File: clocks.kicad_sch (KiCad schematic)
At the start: 19 parts, among them J3 U_FL-R-SMT_10_, U42 CDCE906PWR, Y5 ABM8G-12.000MHZ-18-D2Y-T, Y6 AX3DCF1-200.0000

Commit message: Updated local libraries
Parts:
- J3: footprint antmicro-footprints:Coax_Conn_U.FL -> K410T-devboard-footprints:Coax_Conn_U.FL; symbol antmicroCoaxialConnectorsRF:U_FL-R-SMT_10_ -> K410T-devboard:U_FL-R-SMT_10_

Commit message: Bump revision to 1.0.0. Update name on schematic and PCB sheets
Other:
- title: K410T devboard -> Kintex 410T devboard

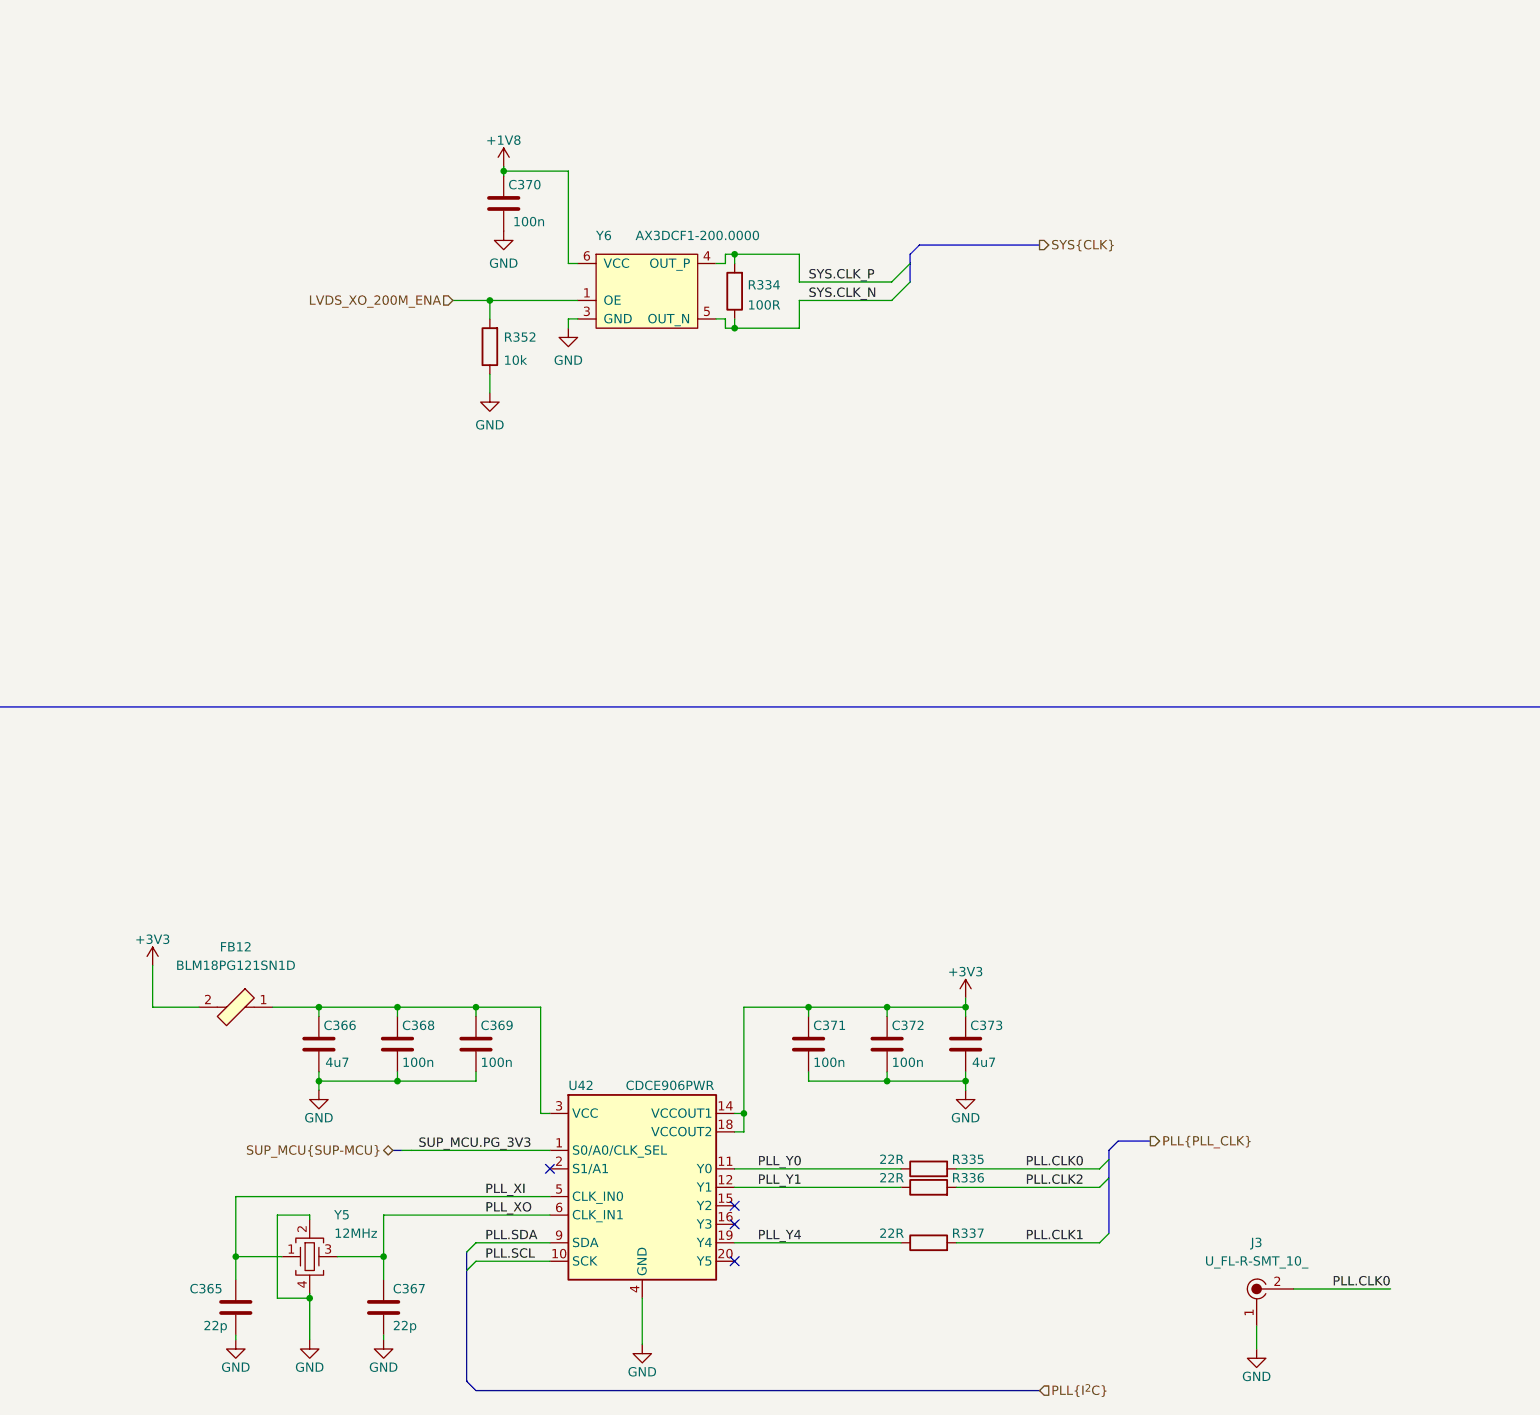
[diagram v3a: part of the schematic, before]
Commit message: Introduce component standardization
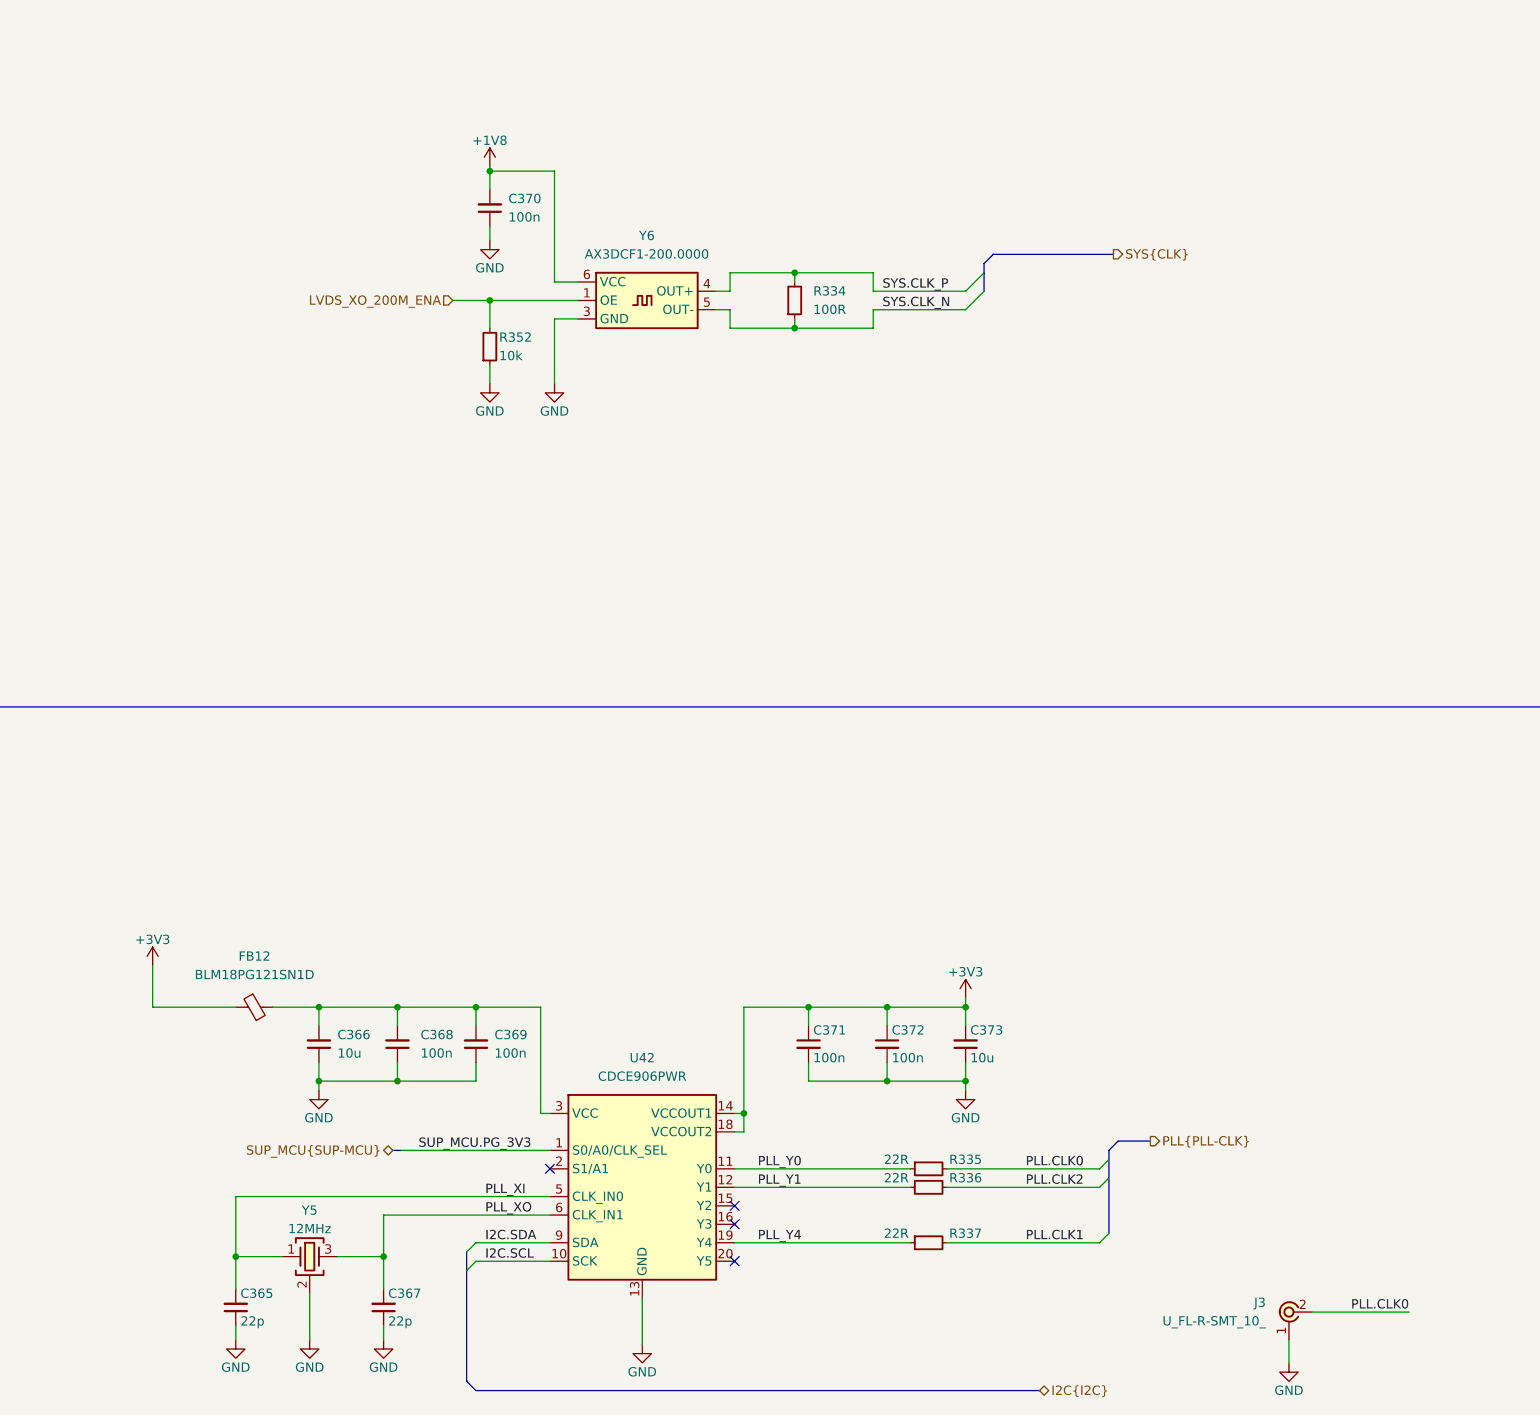
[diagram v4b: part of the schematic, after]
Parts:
- removed C366, C373: C_4u7_0201, K410T-devboard-footprints:0201-cap, symbol K410T-devboard:C_4u7_0201
- added C366, C373: C_10u_0402, K410T-devboard-footprints:C_0402_1005Metric, symbol K410T-devboard:C_10u_0402
- C365, C367: footprint K410T-devboard-footprints:0402-cap -> K410T-devboard-footprints:C_0402_1005Metric; Author (none) -> Antmicro; License (none) -> Apache-2.0; Manufacturer YAGEO -> Yaego
- C368, C369, C370, C371, C372: footprint K410T-devboard-footprints:0402-cap -> K410T-devboard-footprints:C_0402_1005Metric; Author (none) -> Antmicro; Dielectric (none) -> X5R; License (none) -> Apache-2.0; Voltage (none) -> 50V
- FB12: value BLM18PG121SN1D -> FB_120Z_2A_0603; footprint K410T-devboard-footprints:0603-res -> K410T-devboard-footprints:FB_0603_1608Metric; symbol K410T-devboard:BLM18PG121SN1D -> K410T-devboard:FB_120Z_2A_0603; Author (none) -> Antmicro; License (none) -> Apache-2.0; Manufacturer Murata Electronics North America -> Murata
- J3: Author (none) -> Antmicro; License (none) -> Apache-2.0; Manufacturer Hirose Electric Co Ltd -> Hirose
- R334: footprint K410T-devboard-footprints:0402-res -> K410T-devboard-footprints:R_0402_1005Metric; Author (none) -> Antmicro; License (none) -> Apache-2.0; Manufacturer BOURNS -> Bourns; Tolerance (none) -> 1%
- R335, R336, R337: footprint K410T-devboard-footprints:0402-res -> K410T-devboard-footprints:R_0402_1005Metric; Author (none) -> Antmicro; License (none) -> Apache-2.0; MPN CRCW040222R0FKED -> CR0402-FX-22R0GLF; Manufacturer VISHAY -> Bourns; Tolerance (none) -> 1%
- R352: footprint K410T-devboard-footprints:0402-res -> K410T-devboard-footprints:R_0402_1005Metric; Author (none) -> Antmicro; License (none) -> Apache-2.0; MPN CRCW040210K0FKEDHP -> CR0402-FX-1002GLF; Manufacturer VISHAY -> Bourns; Tolerance (none) -> 1%
- U42: Author (none) -> Antmicro; License (none) -> Apache-2.0
- Y5: value ABM8G-12.000MHZ-18-D2Y-T -> Oscillator_SMD_12MHz_KX-7; footprint K410T-devboard-footprints:KX-7 -> K410T-devboard-footprints:Oscillator_SMD_Geyer_KX-7-4Pin_3.2x2.5mm; symbol K410T-devboard:ABM8G-12.000MHZ-18-D2Y-T -> K410T-devboard:Oscillator_SMD_12MHz_KX-7; Author (none) -> Antmicro; License (none) -> Apache-2.0
- Y6: footprint K410T-devboard-footprints:AX3DAF1 -> K410T-devboard-footprints:Oscillator_SMD_Abracon_AX3_3.2x2.5x1mm; Author (none) -> Antmicro; License (none) -> Apache-2.0; Manufacturer ABRACON -> Abracon
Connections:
- net +1V8: now also C370.2; no longer C370.1
- net +3V3: now also C373.2
- net GND: now also C365.1, C367.1, C368.1, C369.1, C370.1, C366.1, C373.1; no longer C365.2, C367.2, C368.2, C369.2, C370.2
- net PLL_XI: now also C365.2; no longer C365.1
- net PLL_XO: now also C367.2; no longer C367.1
- net at FB12.1, U42.3 (VCC), U42.7 (VCC): now also C368.2, C369.2, C366.2; no longer C368.1, C369.1
- net PLL.SCL renamed I2C.SCL
- net PLL.SDA renamed I2C.SDA
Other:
- moved on the sheet: C365, C367, C368, C369, C370, C371, C372, R334

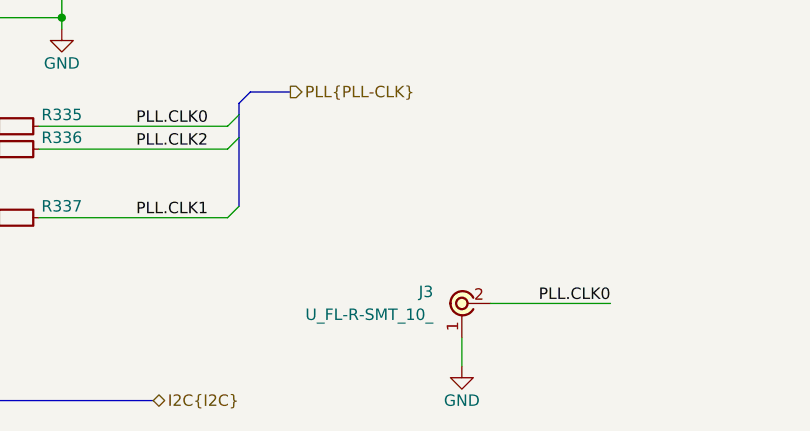
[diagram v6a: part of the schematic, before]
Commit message: [#55729] Fix U_FL-R-SMT_10_
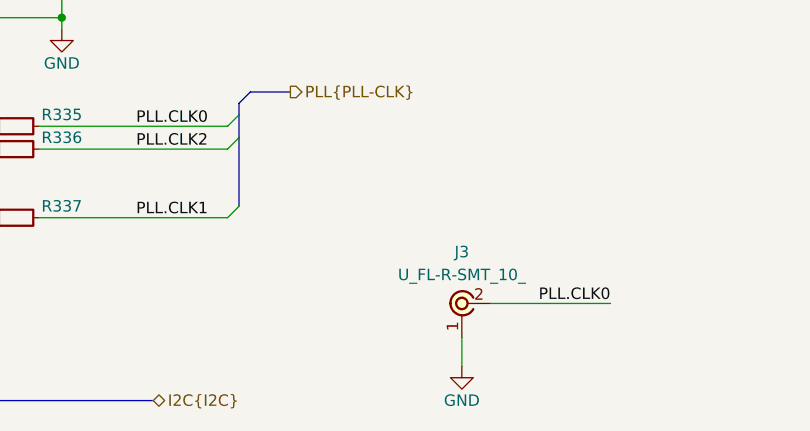
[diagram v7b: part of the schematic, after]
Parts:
- J3: footprint K410T-devboard-footprints:Coax_Conn_U.FL -> antmicro-footprints:Coax_Conn_U.FL; symbol K410T-devboard:U_FL-R-SMT_10_ -> antmicroCoaxialConnectorsRF:U_FL-R-SMT_10_; Manufacturer Hirose -> Hirose Electric
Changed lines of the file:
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@@
     )
   )
-  (symbol (lib_id "K410T-devboard:U_FL-R-SMT_10_") (at 309.88 221.615 0) (unit 1)
+  (symbol (lib_id "antmicroCoaxialConnectorsRF:U_FL-R-SMT_10_") (at 309.88 221.615 0) (unit 1)
     (in_bom yes) (on_board yes) (dnp no) (fields_autoplaced)
-    (property "Reference" "J3" (at 306.705 216.5137 0)
-      (effects (font (size 1.27 1.27)) (justify right))
+    (property "Reference" "J3" (at 309.8799 212.09 0)
+      (effects (font (size 1.27 1.27)))
     )
-    (property "Value" "U_FL-R-SMT_10_" (at 306.705 219.0537 0)
-      (effects (font (size 1.27 1.27) (thickness 0.15)) (justify right))
+    (property "Value" "U_FL-R-SMT_10_" (at 309.8799 214.63 0)
+      (effects (font (size 1.27 1.27) (thickness 0.15)))
     )
-    (property "Footprint" "K410T-devboard-footprints:Coax_Conn_U.FL" (at 327.66 231.775 0)
+    (property "Footprint" "antmicro-footprints:Coax_Conn_U.FL" (at 327.66 231.775 0)
       (effects (font (size 1.27 1.27) (thickness 0.15)) (justify left bottom) hide)
     )
@@
       (effects (font (size 1.27 1.27) (thickness 0.15)) (justify left bottom) hide)
     )
-    (property "Manufacturer" "Hirose" (at 327.66 239.395 0)
+    (property "Manufacturer" "Hirose Electric" (at 327.66 239.395 0)
       (effects (font (size 1.27 1.27) (thickness 0.15)) (justify left bottom) hide)
     )
